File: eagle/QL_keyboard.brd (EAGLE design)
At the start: 66 x 51.4 mm, 42 parts, among them J1 USB-A-S, J2 AVR_SPI_PRG_6TESTPOINTS, U2 3.3V/150mA, U3 MAX3421ESMD, U4 ATMEGA328P_TQFP, U5 TXB0108PW-TSSOP20, Y1 8MHZ

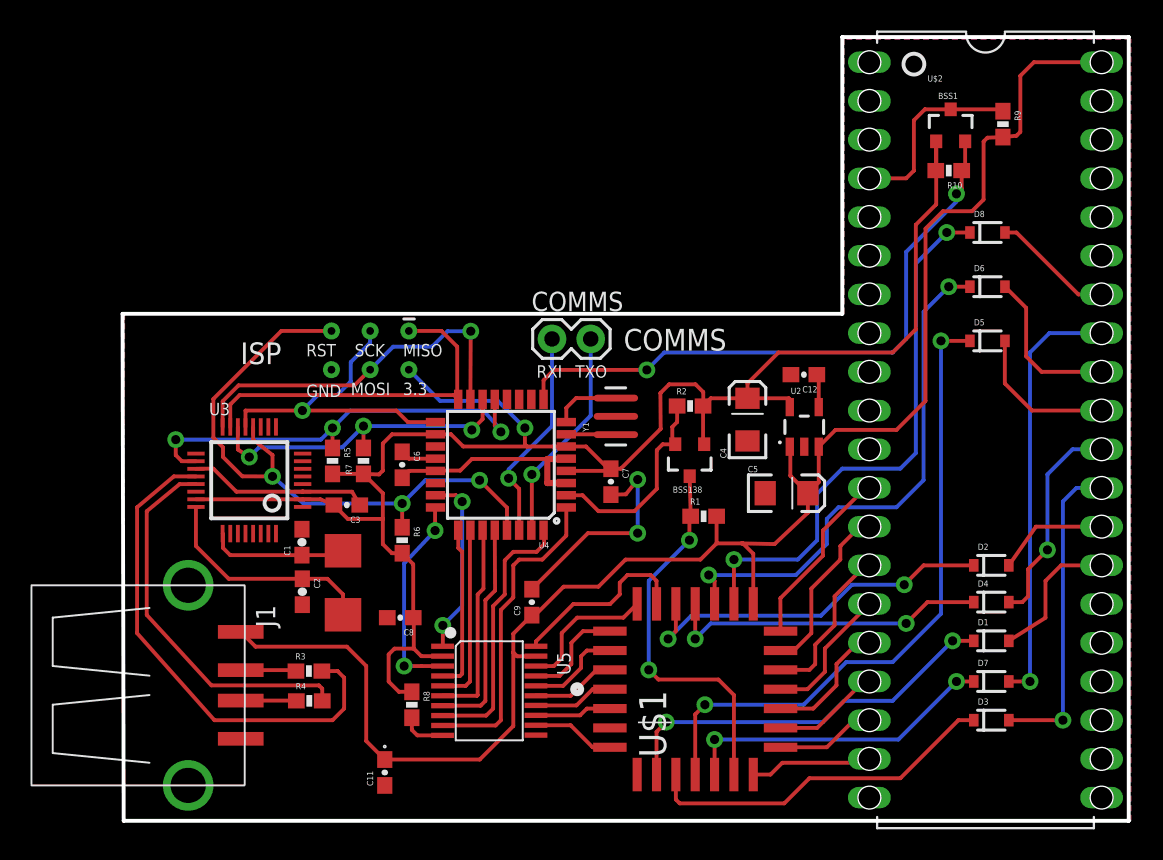
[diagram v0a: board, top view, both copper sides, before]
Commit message: Minor routing adjustments
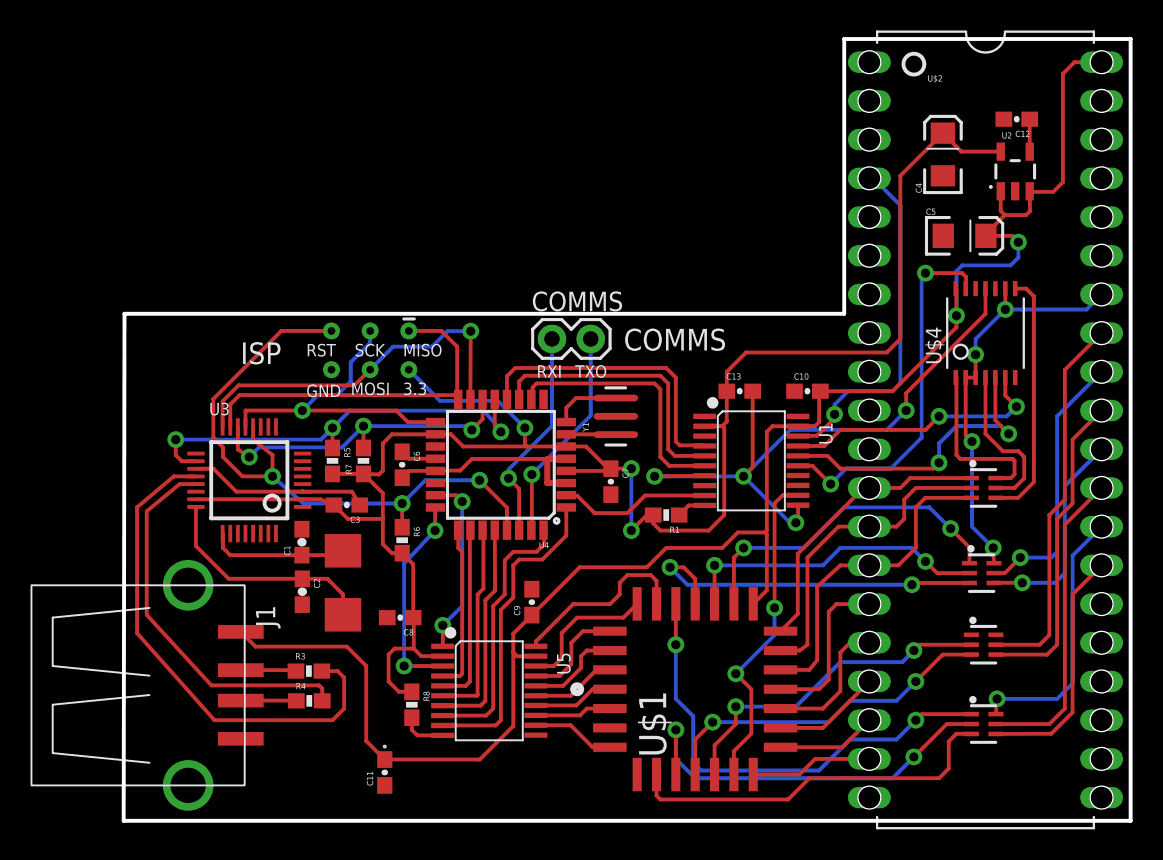
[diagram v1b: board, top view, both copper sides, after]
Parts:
- removed BSS1, BSS138: 200mA/50V, SparkFun-DiscreteSemi:SOT23-3
- removed D1, D2, D3, D4, D5, D6, D7, D8: BAT20J, SparkFun-DiscreteSemi:SOD-323
- removed R10, R2, R9: 10K, SparkFun-Resistors:0603-RES
- added C10, C13: 0.1uF, SparkFun-Capacitors:0603-CAP
- added U$4: 74LVC4066, ppe_custom:TSSOP14
- added U$5, U$6, U$7, U$8: RB530XN, ppe_custom:SOT363
- added U1: TXB0108PW-TSSOP20, Seeed-OPL-ic:TSSOP20-0.65-6.5X4.4MM
- R1: value 10K -> 2.2k
- moved C12 21.8 mm to (72.4, 46.0)
- moved U2 21.7 mm to (72.3, 42.6)
- moved C4 21.6 mm to (67.6, 43.7)
- moved C5 20.5 mm to (69.0, 38.4)
- moved R1 2.46 mm to (49.4, 20.1), turned to 180 degrees
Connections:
- new net ALT: U$4.6, U1.17
- new net ALT33: U1.4, U4.12
- new net CTRL: U$4.5, U1.16
- new net CTRL33: U1.5, U4.11
- new net N$27: U$4.1, U$8.6
- new net N$28: U$4.4, U$8.5
- new net N$29: U$4.8, U$8.4
- new net N$31: R1.1, U1.10
- new net SHFT: U$4.13, U1.15
- new net SHFT33: U1.6, U4.10
- net 3.3V: now also C13.1, R1.2, U1.2; no longer BSS1.1, BSS138.1, R10.2, R2.2
- net GND: now also C10.1, C13.2, U$4.10, U$4.11, U$4.12, U$4.7, U1.1, U1.11, U1.13, U1.14, U1.20, U1.7, U1.8
- net N$19: now also U$5.3; no longer D1.C
- net N$20: now also U$5.1; no longer D2.C
- net N$21: now also U$5.2; no longer D3.C
- net N$22: now also U$7.3; no longer D4.C
- net N$23: now also U$6.3; no longer D5.C
- net N$24: now also U$7.2; no longer D6.C
- net N$25: now also U$6.2; no longer D7.C
- net N$26: now also U$7.1; no longer D8.C
- net RST8808V33: now also U1.9; no longer BSS138.2, R2.1
- net RST8808V5: now also U1.12; no longer BSS138.3, R1.1
- net RSTQL: now also U1.18; no longer BSS1.3, R9.1
- net RSTQLV33: no longer BSS1.2, R10.1
- net VCC: now also C10.2, U$4.14, U1.19; no longer R1.2, R9.2
- net X0: now also U$5.4; no longer D1.A
- net X1: now also U$5.6; no longer D2.A
- net X2: now also U$5.5; no longer D3.A
- net X3: now also U$7.4; no longer D4.A
- net X4: now also U$6.4; no longer D5.A
- net X5: now also U$7.5; no longer D6.A
- net X6: now also U$6.5; no longer D7.A
- net X7: now also U$4.2, U$4.3, U$4.9, U$7.6; no longer D8.A
- net Y0: now also U$8.1
- net Y1: now also U$8.2
- net Y2: now also U$8.3
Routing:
- net RSTQLV33: track 40.7 -> 0.00 mm, vias 2 -> 0
- net GND: track 40.3 -> 69.5 mm, vias 2 -> 4
- net SHFT: track 0.00 -> 24.3 mm, vias 0 -> 2
- net CTRL: track 0.00 -> 20.3 mm, vias 0 -> 2
- net N$23: track 42.6 -> 22.7 mm
- net ALT33: track 0.00 -> 19.3 mm
- net X7: track 8.03 -> 27.0 mm, vias 0 -> 4
- net CTRL33: track 0.00 -> 18.2 mm
- net ALT: track 0.00 -> 17.6 mm, vias 0 -> 2
- net SHFT33: track 0.00 -> 17.0 mm
- net N$29: track 0.00 -> 16.5 mm
- net N$26: track 36.4 -> 22.0 mm
- net N$24: track 34.5 -> 20.4 mm
- net N$27: track 0.00 -> 11.3 mm
- net Y2: track 10.5 -> 21.6 mm
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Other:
- board size 66 x 51.4 mm -> 66.1 x 51.3 mm
- board text added: "USB Keyboard Adapter For the Sinclair QL (c) 2016 Petri Pellinen https://github.com/ppe/QL_USB_Keyboard v 1.0"
- board text removed: "USB Keyboard Adapter For the Sinclair QL (c) 2016 Petri Pellinen https://github.com/ppe/QL_USB_Keyboard v 0.3"

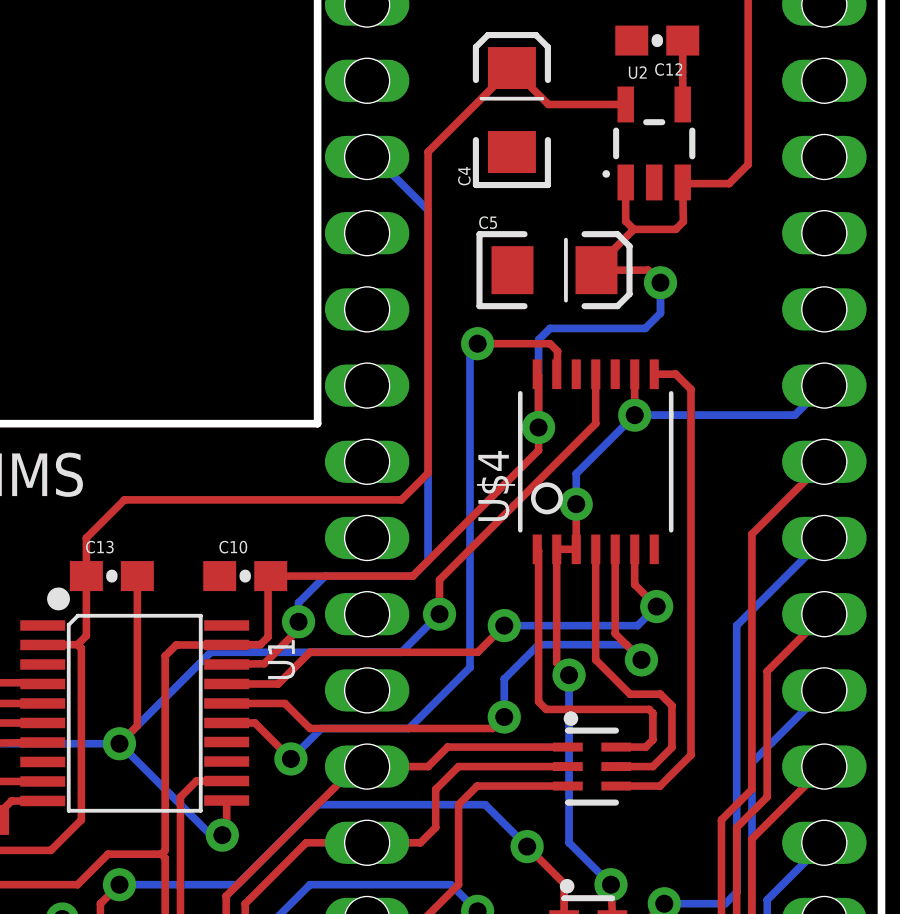
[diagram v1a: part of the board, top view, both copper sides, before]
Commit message: Minor routing change in board.
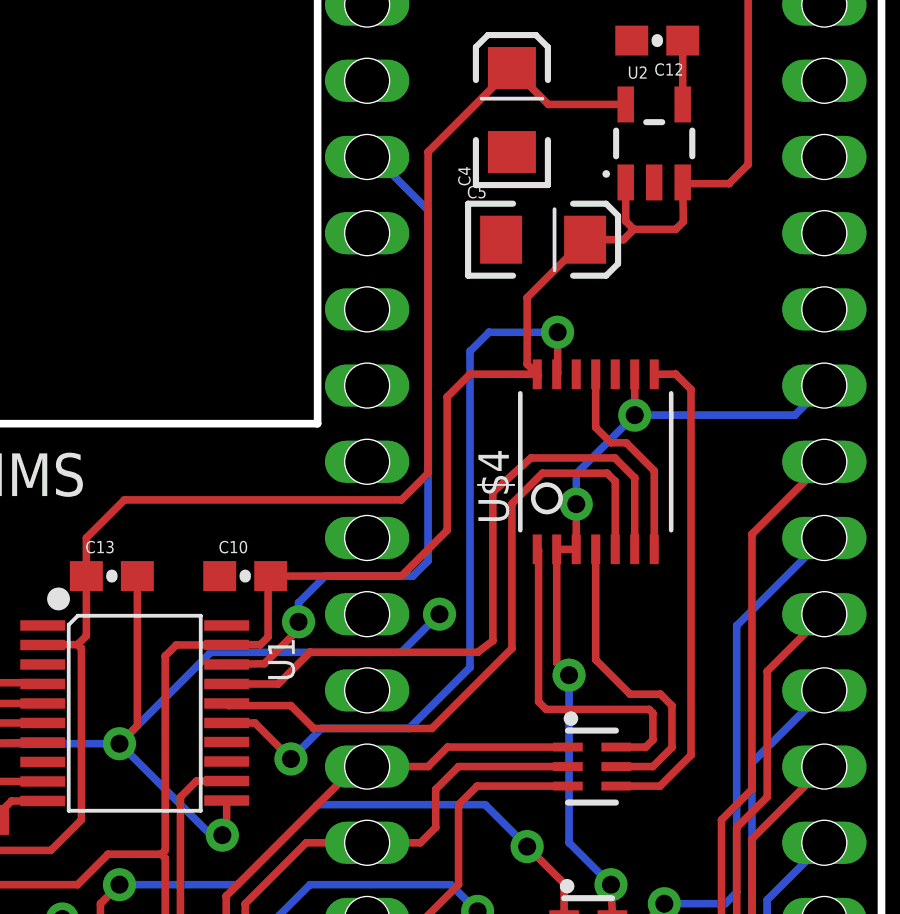
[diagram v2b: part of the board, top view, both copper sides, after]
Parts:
- moved C5 1.09 mm to (68.6, 39.4)
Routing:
- net ALT: track 17.6 -> 22.2 mm, vias 2 -> 0
- net VCC: track 113.0 -> 108.7 mm, vias 2 -> 0
- net GND: track 69.5 -> 66.3 mm
- net CTRL: track 20.3 -> 22.0 mm, vias 2 -> 0
- net SHFT: track 24.3 -> 25.0 mm
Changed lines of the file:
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@@
 <attribute name="PROD_ID" value="CAP-07888" x="72.409" y="46.044" size="0.8128" layer="27" font="vector" rot="R180" display="off"/>
 </element>
-<element name="C5" library="SparkFun-Capacitors" package="EIA3216" value="10uF" x="68.984" y="38.391">
-<attribute name="PROD_ID" value="CAP-00811" x="68.984" y="38.391" size="0.8128" layer="27" font="vector" display="off"/>
+<element name="C5" library="SparkFun-Capacitors" package="EIA3216" value="10uF" x="68.603" y="39.407">
+<attribute name="PROD_ID" value="CAP-00811" x="68.603" y="39.407" size="0.8128" layer="27" font="vector" display="off"/>
 </element>
 <element name="C4" library="SparkFun-Capacitors" package="EIA3216" value="10uF" x="67.564" y="43.728" rot="R90">
@@
 <wire x1="73.025" y1="39.751" x2="73.279" y2="40.005" width="0.254" layer="1"/>
 <wire x1="73.279" y1="40.005" x2="73.2574" y2="41.3149" width="0.254" layer="1"/>
-<wire x1="70.384" y1="38.391" x2="70.384" y2="38.507" width="0.254" layer="1"/>
-<wire x1="70.384" y1="38.507" x2="71.628" y2="39.751" width="0.254" layer="1"/>
-<wire x1="70.384" y1="38.391" x2="72.099" y2="38.391" width="0.254" layer="1"/>
-<wire x1="72.099" y1="38.391" x2="72.517" y2="37.973" width="0.254" layer="1"/>
-<via x="72.517" y="37.973" extent="1-16" drill="0.6"/>
-<wire x1="72.517" y1="37.973" x2="72.517" y2="36.957" width="0.254" layer="16"/>
-<wire x1="72.517" y1="36.957" x2="72.009" y2="36.449" width="0.254" layer="16"/>
-<wire x1="72.009" y1="36.449" x2="68.834" y2="36.449" width="0.254" layer="16"/>
-<wire x1="68.834" y1="36.449" x2="68.453" y2="36.068" width="0.254" layer="16"/>
-<wire x1="68.453" y1="36.068" x2="68.453" y2="33.147" width="0.254" layer="16"/>
-<via x="68.453" y="33.147" extent="1-16" drill="0.6"/>
-<wire x1="68.453" y1="33.147" x2="68.453" y2="34.8768" width="0.254" layer="1"/>
 <wire x1="68.453" y1="34.8768" x2="68.408" y2="34.9218" width="0.254" layer="1"/>
-<wire x1="64.262" y1="28.194" x2="68.453" y2="32.385" width="0.254" layer="1"/>
-<wire x1="68.453" y1="32.385" x2="68.453" y2="33.147" width="0.254" layer="1"/>
 <wire x1="59.436" y1="26.162" x2="59.182" y2="25.908" width="0.254" layer="1"/>
 <wire x1="59.182" y1="25.908" x2="58.056" y2="25.897" width="0.254" layer="1"/>
-<wire x1="64.262" y1="28.194" x2="59.524" y2="28.194" width="0.254" layer="1"/>
 <wire x1="58.056" y1="25.897" x2="56.377" y2="25.897" width="0.254" layer="1"/>
 <wire x1="56.377" y1="25.897" x2="56.007" y2="25.527" width="0.254" layer="1"/>
@@
 <wire x1="59.436" y1="26.162" x2="59.436" y2="28.106" width="0.254" layer="1"/>
 <wire x1="59.436" y1="28.106" x2="59.524" y2="28.194" width="0.254" layer="1"/>
+<wire x1="65.405" y1="34.163" x2="65.405" y2="29.718" width="0.254" layer="1"/>
+<wire x1="65.405" y1="29.718" x2="63.881" y2="28.194" width="0.254" layer="1"/>
+<wire x1="63.881" y1="28.194" x2="59.524" y2="28.194" width="0.254" layer="1"/>
+<wire x1="71.628" y1="39.751" x2="71.284" y2="39.407" width="0.254" layer="1"/>
+<wire x1="71.284" y1="39.407" x2="70.003" y2="39.407" width="0.254" layer="1"/>
+<wire x1="70.003" y1="39.407" x2="68.072" y2="37.476" width="0.254" layer="1"/>
+<wire x1="68.072" y1="37.476" x2="68.072" y2="35.2578" width="0.254" layer="1"/>
+<wire x1="68.072" y1="35.2578" x2="68.408" y2="34.9218" width="0.254" layer="1"/>
+<wire x1="65.405" y1="34.163" x2="66.167" y2="34.925" width="0.254" layer="1"/>
+<wire x1="66.167" y1="34.925" x2="68.408" y2="34.9218" width="0.254" layer="1"/>
 </signal>
 <signal name="GND">
@@
 <wire x1="63.881" y1="25.654" x2="65.151" y2="26.924" width="0.254" layer="16"/>
 <via x="65.151" y="26.924" extent="1-16" drill="0.6"/>
-<wire x1="65.151" y1="26.924" x2="65.151" y2="28.067" width="0.254" layer="1"/>
-<wire x1="65.151" y1="28.067" x2="70.358" y2="33.274" width="0.254" layer="1"/>
-<wire x1="70.358" y1="33.274" x2="70.358" y2="34.9218" width="0.254" layer="1"/>
 <wire x1="55.079" y1="23.202" x2="54.483" y2="22.606" width="0.254" layer="1"/>
+<wire x1="72.308" y1="29.0862" x2="72.308" y2="31.705" width="0.254" layer="1"/>
+<wire x1="70.358" y1="33.147" x2="70.358" y2="34.9218" width="0.254" layer="1"/>
+<wire x1="72.308" y1="31.705" x2="71.374" y2="32.639" width="0.254" layer="1"/>
+<wire x1="71.374" y1="32.639" x2="70.866" y2="32.639" width="0.254" layer="1"/>
+<wire x1="70.866" y1="32.639" x2="70.358" y2="33.147" width="0.254" layer="1"/>
 </signal>
 <signal name="3.3V">
@@
 <wire x1="64.135" y1="23.114" x2="66.167" y2="25.146" width="0.254" layer="16"/>
 <wire x1="66.167" y1="25.146" x2="66.167" y2="35.687" width="0.254" layer="16"/>
-<wire x1="66.167" y1="35.687" x2="66.421" y2="35.941" width="0.254" layer="16"/>
-<via x="66.421" y="35.941" extent="1-16" drill="0.6"/>
-<wire x1="66.421" y1="35.941" x2="68.834" y2="35.941" width="0.254" layer="1"/>
-<wire x1="68.834" y1="35.941" x2="69.088" y2="35.687" width="0.254" layer="1"/>
-<wire x1="69.088" y1="35.687" x2="69.058" y2="34.9218" width="0.254" layer="1"/>
+<via x="69.088" y="36.322" extent="1-16" drill="0.6"/>
+<wire x1="69.058" y1="34.9218" x2="69.088" y2="34.9518" width="0.254" layer="1"/>
+<wire x1="69.088" y1="34.9518" x2="69.088" y2="36.322" width="0.254" layer="1"/>
+<wire x1="66.167" y1="35.687" x2="66.802" y2="36.322" width="0.254" layer="16"/>
+<wire x1="66.802" y1="36.322" x2="69.088" y2="36.322" width="0.254" layer="16"/>
 </signal>
 <signal name="CTRL">
 <contactref element="U1" pad="16"/>
 <contactref element="U$4" pad="5"/>
-<wire x1="58.056" y1="23.947" x2="60" y2="23.947" width="0.254" layer="1"/>
-<wire x1="60" y1="23.947" x2="60.833" y2="23.114" width="0.254" layer="1"/>
-<wire x1="60.833" y1="23.114" x2="66.929" y2="23.114" width="0.254" layer="1"/>
-<wire x1="66.929" y1="23.114" x2="67.31" y2="23.495" width="0.254" layer="1"/>
-<via x="67.31" y="23.495" extent="1-16" drill="0.6"/>
-<via x="71.882" y="25.4" extent="1-16" drill="0.6"/>
-<wire x1="71.882" y1="25.4" x2="71.008" y2="26.274" width="0.254" layer="1"/>
-<wire x1="71.008" y1="26.274" x2="71.008" y2="29.0862" width="0.254" layer="1"/>
-<wire x1="68.453" y1="25.908" x2="67.31" y2="24.765" width="0.254" layer="16"/>
-<wire x1="67.31" y1="24.765" x2="67.31" y2="23.495" width="0.254" layer="16"/>
-<wire x1="68.453" y1="25.908" x2="71.374" y2="25.908" width="0.254" layer="16"/>
-<wire x1="71.374" y1="25.908" x2="71.882" y2="25.4" width="0.254" layer="16"/>
+<wire x1="71.008" y1="29.0862" x2="71.008" y2="31.354" width="0.254" layer="1"/>
+<wire x1="71.008" y1="31.354" x2="70.739" y2="31.623" width="0.254" layer="1"/>
+<wire x1="70.739" y1="31.623" x2="68.58" y2="31.623" width="0.254" layer="1"/>
+<wire x1="68.58" y1="31.623" x2="67.564" y2="30.607" width="0.254" layer="1"/>
+<wire x1="67.564" y1="30.607" x2="67.564" y2="25.781" width="0.254" layer="1"/>
+<wire x1="67.564" y1="25.781" x2="64.897" y2="23.114" width="0.254" layer="1"/>
+<wire x1="64.897" y1="23.114" x2="60.96" y2="23.114" width="0.254" layer="1"/>
+<wire x1="60.96" y1="23.114" x2="60.198" y2="23.876" width="0.254" layer="1"/>
+<wire x1="60.198" y1="23.876" x2="58.127" y2="23.876" width="0.254" layer="1"/>
+<wire x1="58.127" y1="23.876" x2="58.056" y2="23.947" width="0.254" layer="1"/>
 </signal>
 <signal name="ALT">
@@
 <wire x1="59.776" y1="24.597" x2="60.833" y2="25.654" width="0.254" layer="1"/>
 <wire x1="60.833" y1="25.654" x2="66.421" y2="25.654" width="0.254" layer="1"/>
-<wire x1="66.421" y1="25.654" x2="67.31" y2="26.543" width="0.254" layer="1"/>
-<via x="67.31" y="26.543" extent="1-16" drill="0.6"/>
-<wire x1="67.31" y1="26.543" x2="71.755" y2="26.543" width="0.254" layer="16"/>
-<wire x1="71.755" y1="26.543" x2="72.39" y2="27.178" width="0.254" layer="16"/>
-<via x="72.39" y="27.178" extent="1-16" drill="0.6"/>
-<wire x1="72.39" y1="27.178" x2="71.658" y2="27.91" width="0.254" layer="1"/>
-<wire x1="71.658" y1="27.91" x2="71.658" y2="29.0862" width="0.254" layer="1"/>
+<wire x1="68.199" y1="32.131" x2="66.929" y2="30.988" width="0.254" layer="1"/>
+<wire x1="66.929" y1="30.988" x2="66.929" y2="26.035" width="0.254" layer="1"/>
+<wire x1="66.929" y1="26.035" x2="66.421" y2="25.654" width="0.254" layer="1"/>
+<wire x1="71.658" y1="29.0862" x2="71.658" y2="31.466" width="0.254" layer="1"/>
+<wire x1="71.658" y1="31.466" x2="70.993" y2="32.131" width="0.254" layer="1"/>
+<wire x1="70.993" y1="32.131" x2="68.199" y2="32.131" width="0.254" layer="1"/>
 </signal>
 </signals>
